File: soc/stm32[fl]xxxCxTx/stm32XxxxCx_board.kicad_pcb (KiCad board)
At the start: 2 copper layers, 38.1 x 58.4 mm, 33 parts, among them U1 STM32F103CBTx, Y1 8MHz, 20pF, Y2 32KHz, 4pF

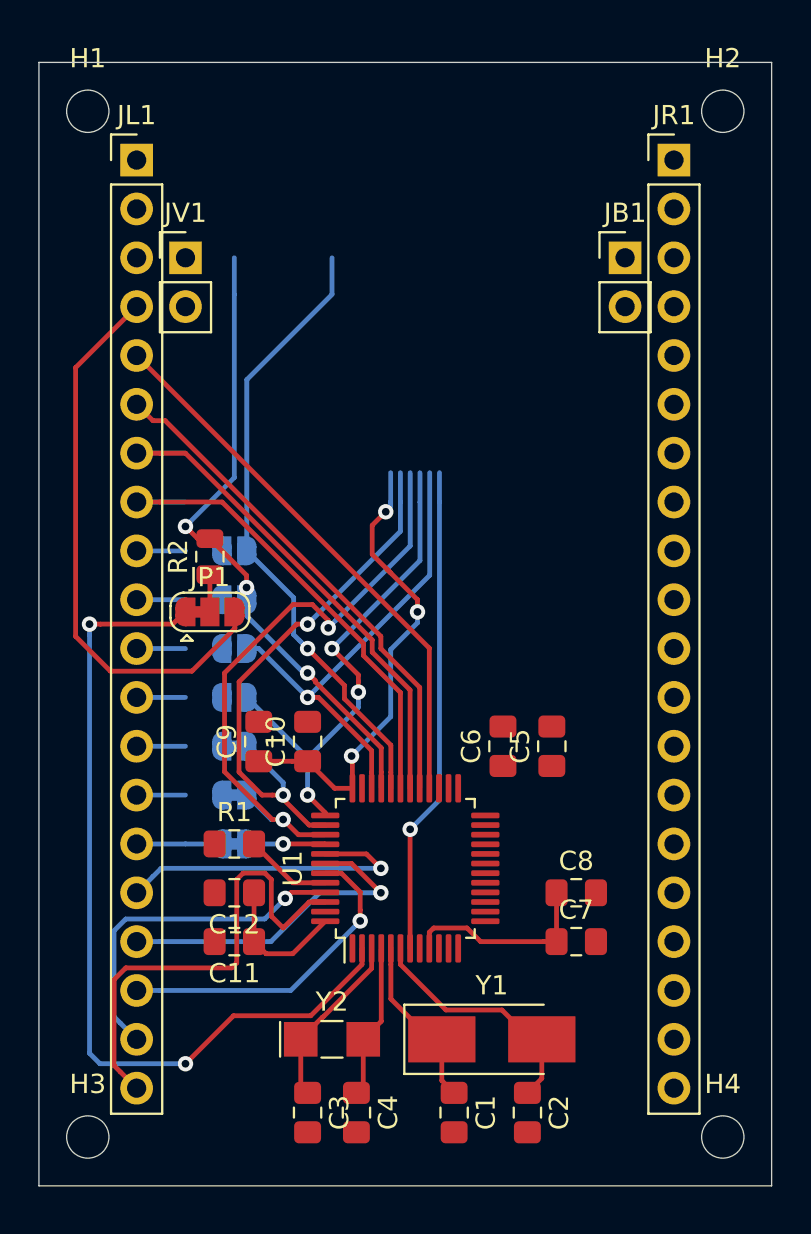
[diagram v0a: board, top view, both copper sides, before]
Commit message: Defining areas and connections per 'module'
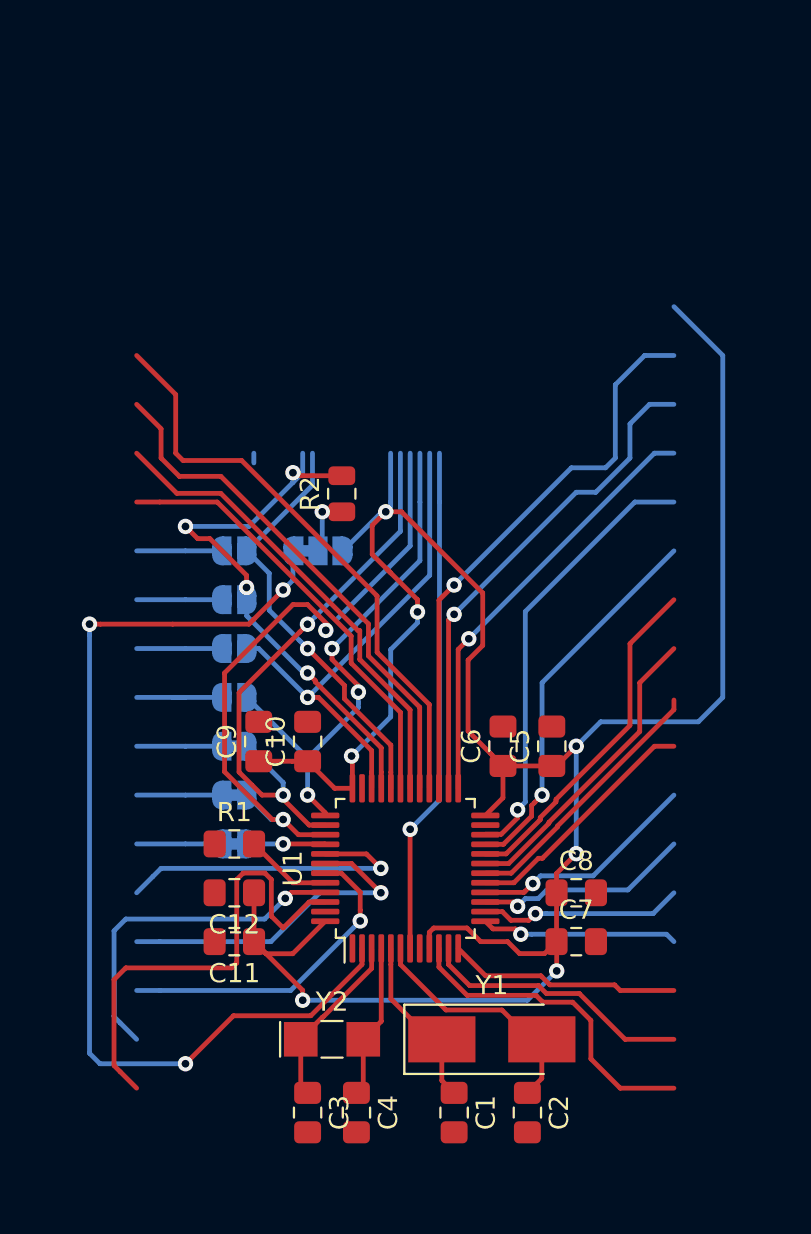
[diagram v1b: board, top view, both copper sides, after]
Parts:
- removed H1, H2, H3, H4: MountingHole, MountingHole:MountingHole_2.2mm_M2_ISO7380
- removed JB1, JV1: Conn_01x02, Connector_PinHeader_2.54mm:PinHeader_1x02_P2.54mm_Vertical
- removed JL1, JR1: Conn_01x20, Connector_PinHeader_2.54mm:PinHeader_1x20_P2.54mm_Vertical
- JP1: moved to B.Cu
- moved R2 7.60 mm to (147.8, 73.2)
- moved JP1 6.45 mm to (146.6, 76.2)
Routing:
- net VDD: track 71.8 -> 129.2 mm, vias 3 -> 7
- net PB14: track 0.00 -> 29.5 mm, vias 0 -> 1
- net PB13: track 0.00 -> 26.2 mm, vias 0 -> 1
- net PB11: track 0.00 -> 23.0 mm, vias 0 -> 1
- net PB12: track 0.00 -> 22.7 mm, vias 0 -> 1
- net PB10: track 0.00 -> 19.9 mm, vias 0 -> 1
- net PB2: track 0.00 -> 17.9 mm
- net PA0: track 0.00 -> 17.0 mm
- net PB1: track 0.00 -> 16.0 mm
- net PA1: track 0.00 -> 14.2 mm
- net PB0: track 0.00 -> 13.9 mm
- net PA7: track 0.00 -> 12.7 mm
- net PA2: track 0.00 -> 12.1 mm
- net PA6: track 0.00 -> 11.9 mm, vias 0 -> 1
- net PA5: track 0.00 -> 11.2 mm, vias 0 -> 1
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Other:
- board outline removed

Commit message: Changes after combining
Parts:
- JP1: value SolderJumper_3_Bridged12 -> USBPULL
- JP2: value USB_D- -> PA11
- JP3: value USB_D+ -> PA12
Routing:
- net GND: track 0.00 -> 27.1 mm, vias 0 -> 7
- net L14: track 16.9 -> 17.7 mm
- net PB3: track 31.9 -> 32.6 mm
- net VDD: track 129.2 -> 128.7 mm
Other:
- board text added: "PC13"
- board text added: "VDD"
